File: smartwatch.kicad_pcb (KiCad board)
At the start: 2 copper layers, 40 x 40 mm, 42 parts, among them IC2 NORA-B120-00B, J1 Conn_01x01_Pin, J2 Conn_01x01_Pin, J3 5022441530, J5 Conn_01x06_Pin, Q1 2N7002-7-F, U1 MAX17048G+T10, U10 AP2127K-1.8, U2 AP2112K-3.3TRG1, U3 MAX30102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

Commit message: charging circuit complete
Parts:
- removed BT1: Battery_Cell, Capacitor_SMD:C_1812_4532Metric
- removed C10, C6: 100uF, Capacitor_SMD:C_0402_1005Metric
- removed C2: 1uF, Capacitor_SMD:C_0402_1005Metric
- removed D1: LED_GREEN, LED_SMD:LED_0402_1005Metric
- removed J5: Conn_01x06_Pin, Connector_PinHeader_2.54mm:PinHeader_1x06_P2.54mm_Vertical
- removed R1: 3.3k, Resistor_SMD:R_0402_1005Metric
- removed R12: 470, Resistor_SMD:R_0402_1005Metric
- removed R6: 5.1k, Resistor_SMD:R_0402_1005Metric
- removed U2: AP2112K-3.3TRG1, AP2112K-3-3TRG1:SOT_RG1_DIO
- removed U7: MCP73831-2-OT, Package_TO_SOT_SMD:SOT-23-5
- added BT3: Battery_Cell, Capacitor_SMD:C_1812_4532Metric, F.Cu at (149.9, 105.8)
- added C15: 100uF, Capacitor_SMD:C_0402_1005Metric, F.Cu at (158.3, 88.3)
- added C16: 4.7uF, Capacitor_Tantalum_SMD:CP_EIA-2012-12_Kemet-R, F.Cu at (159.9, 87.5)
- added C18: 0.1uF, Capacitor_SMD:C_0402_1005Metric, F.Cu at (171.3, 106.2)
- added C19: 4.7uF, Capacitor_SMD:C_0402_1005Metric, F.Cu at (146.9, 106.0)
- added D5: LBAT54XV2T1G, Diode_SMD:D_SOD-523, F.Cu at (160.1, 97.0)
- added D6: LED_GREEN, LED_SMD:LED_0402_1005Metric, F.Cu at (144.0, 99.6)
- added IC1: W25N01GVZEIG, W25N01GVZEIG_TR:SON127P800X600X80-9N-D, F.Cu at (167.1, 102.3)
- added J4: Conn_01x03_Pin, Connector_PinSocket_2.54mm:PinSocket_1x03_P2.54mm_Vertical, F.Cu at (168.4, 107.6)
- added J6: Conn_01x01_Pin, Connector_PinSocket_2.54mm:PinSocket_1x01_P2.54mm_Vertical, F.Cu at (159.7, 105.6)
- added Q2: NTR1P02T1G, Package_TO_SOT_SMD:SOT-23, F.Cu at (157.2, 97.3)
- added Q6: NTR1P02T1G, Package_TO_SOT_SMD:SOT-23, F.Cu at (157.2, 100.8)
- added R14: 3.3k, Resistor_SMD:R_0603_1608Metric, F.Cu at (171.0, 82.8)
- added R16: 5.1k, Resistor_SMD:R_0603_1608Metric, F.Cu at (160.5, 102.2)
- added R17: 5.1k, Resistor_SMD:R_0402_1005Metric, F.Cu at (148.0, 101.2)
- added R18: 470, Resistor_SMD:R_0402_1005Metric, F.Cu at (146.2, 99.6)
- added REF**: MountingHole_2.2mm_M2_Pad, MountingHole:MountingHole_2.2mm_M2_Pad, F.Cu at (159.1, 110.3)
- added REF**: MountingHole_2.2mm_M2_Pad, MountingHole:MountingHole_2.2mm_M2_Pad, F.Cu at (159.1, 74.9)
- added U11: MCP73831-2-OT, Package_TO_SOT_SMD:SOT-23-5, F.Cu at (145.1, 101.9)
- C1: value 4.7uF -> 1uF
- J1: value Conn_01x01_Pin -> Charging_Pad-
- J2: value Conn_01x01_Pin -> Charging_Pad+
- Q1: value 2N7002-7-F -> 2N7002
- R13: footprint Resistor_SMD:R_0402_1005Metric -> Resistor_SMD:R_0603_1608Metric
- U3: moved to B.Cu
- U8: value W25Q128JVS -> AP2112K-3.3TRG1; footprint Package_SO:SOIC-8_5.23x5.23mm_P1.27mm -> AP2112K-3-3TRG1:SOT_RG1_DIO
- moved C12 48.5 mm to (153.2, 109.2), turned to -90 degrees
- moved C7 47.6 mm to (155.5, 109.2), turned to -90 degrees
- moved C8 47.2 mm to (154.4, 109.2), turned to -90 degrees
- moved U10 43.1 mm to (154.2, 105.4)
- moved U3 35.7 mm to (159.1, 92.5), turned to 180 degrees
- moved U1 23.7 mm to (174.3, 101.2), turned to 90 degrees
- moved R5 23.2 mm to (153.5, 100.0), turned to -90 degrees
- moved R7 21.5 mm to (152.5, 100.0), turned to -90 degrees
- moved R8 18.3 mm to (149.9, 99.6), turned to 180 degrees
- moved R10 18.2 mm to (147.0, 85.6)
- moved U8 13.6 mm to (159.1, 92.5), turned to 90 degrees
- moved C1 11.8 mm to (153.6, 103.0)
- moved C4 6.72 mm to (178.5, 77.3)
- moved C5 6.72 mm to (178.5, 79.3)
- moved J3 4.00 mm to (159.0, 81.3), turned to 180 degrees
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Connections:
- C1 pad 1: Net-(BT1-+) -> VBUS
- IC2 pad D1: unconnected-(IC2-P0.15/IO2-PadD1) -> /FLASH_IO2
- IC2 pad D2: unconnected-(IC2-P0.13/IO0-PadD2) -> /FLASH_IO0
- IC2 pad E1: unconnected-(IC2-P0.18/CSN-PadE1) -> /FLASH_CS
- IC2 pad E2: unconnected-(IC2-P0.14/IO1-PadE2) -> /FLASH_IO1
- IC2 pad E8: unconnected-(IC2-P0.05/AIN1_-PadE8) -> /BACKLIGHT_EN
- IC2 pad F1: unconnected-(IC2-P0.17/SCK-PadF1) -> /FLASH_CLK
- IC2 pad F2: unconnected-(IC2-P0.16/IO3-PadF2) -> /FLASH_IO3
- IC2 pad G9: unconnected-(IC2-P1.13-PadG9) -> /SCL
- IC2 pad H9: unconnected-(IC2-P1.11_-PadH9) -> /SDA
- J2 pad 1: Net-(D2-A) -> VBUS
- R13 pad 1: /AC_SCL -> /SDA
- R13 pad 2: +3.3V -> VSYS
- U1 pad 1: Net-(BT1-+) -> GND
- U1 pad 2: Net-(BT1-+) -> /BAT+
- U1 pad 3: GND -> /BAT+
- U1 pad 7: /GAUGE_SCL -> /SCL
- U1 pad 8: /GAUGE_SDA -> /SDA
- U10 pad 1: VSYS -> /BAT+
- U3 pad 2: /AC_SCL -> /SCL
- U3 pad 3: /AC_SDA -> /SDA
- U8 pad 1: /FLASH_CS -> Net-(D5-K)
- U8 pad 2: /SD_DO -> GND
- U8 pad 3: /SD_WP -> Net-(D5-K)
- U8 pad 4: GND -> unconnected-(U8-NC-Pad4)
- U8 pad 5: /SD_DI -> VSYS
- U9 pad 1: /AC_SCL -> /SCL
- U9 pad 4: /AC_SDA -> /SDA
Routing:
- net /BAT+: track 0.00 -> 42.3 mm, vias 0 -> 2
- net VBUS: track 0.00 -> 36.3 mm, vias 0 -> 4
- net VSYS: track 8.00 -> 19.1 mm
- net Net-(U10-VOUT): track 0.00 -> 8.22 mm
- net Net-(D5-K): track 0.00 -> 6.96 mm
- net Net-(D2-K): track 6.09 -> 0.00 mm
- net Net-(R8-Pad1): track 0.00 -> 2.70 mm
- net Net-(R7-Pad1): track 0.00 -> 2.65 mm
- net Net-(R5-Pad1): track 0.00 -> 2.64 mm
- net Net-(Q2-D): track 0.00 -> 2.59 mm
- net Net-(U11-PROG): track 0.00 -> 2.04 mm
- net Net-(D6-K): track 0.00 -> 1.58 mm
- net Net-(U5-Pad16): track 0.00 -> 1.00 mm

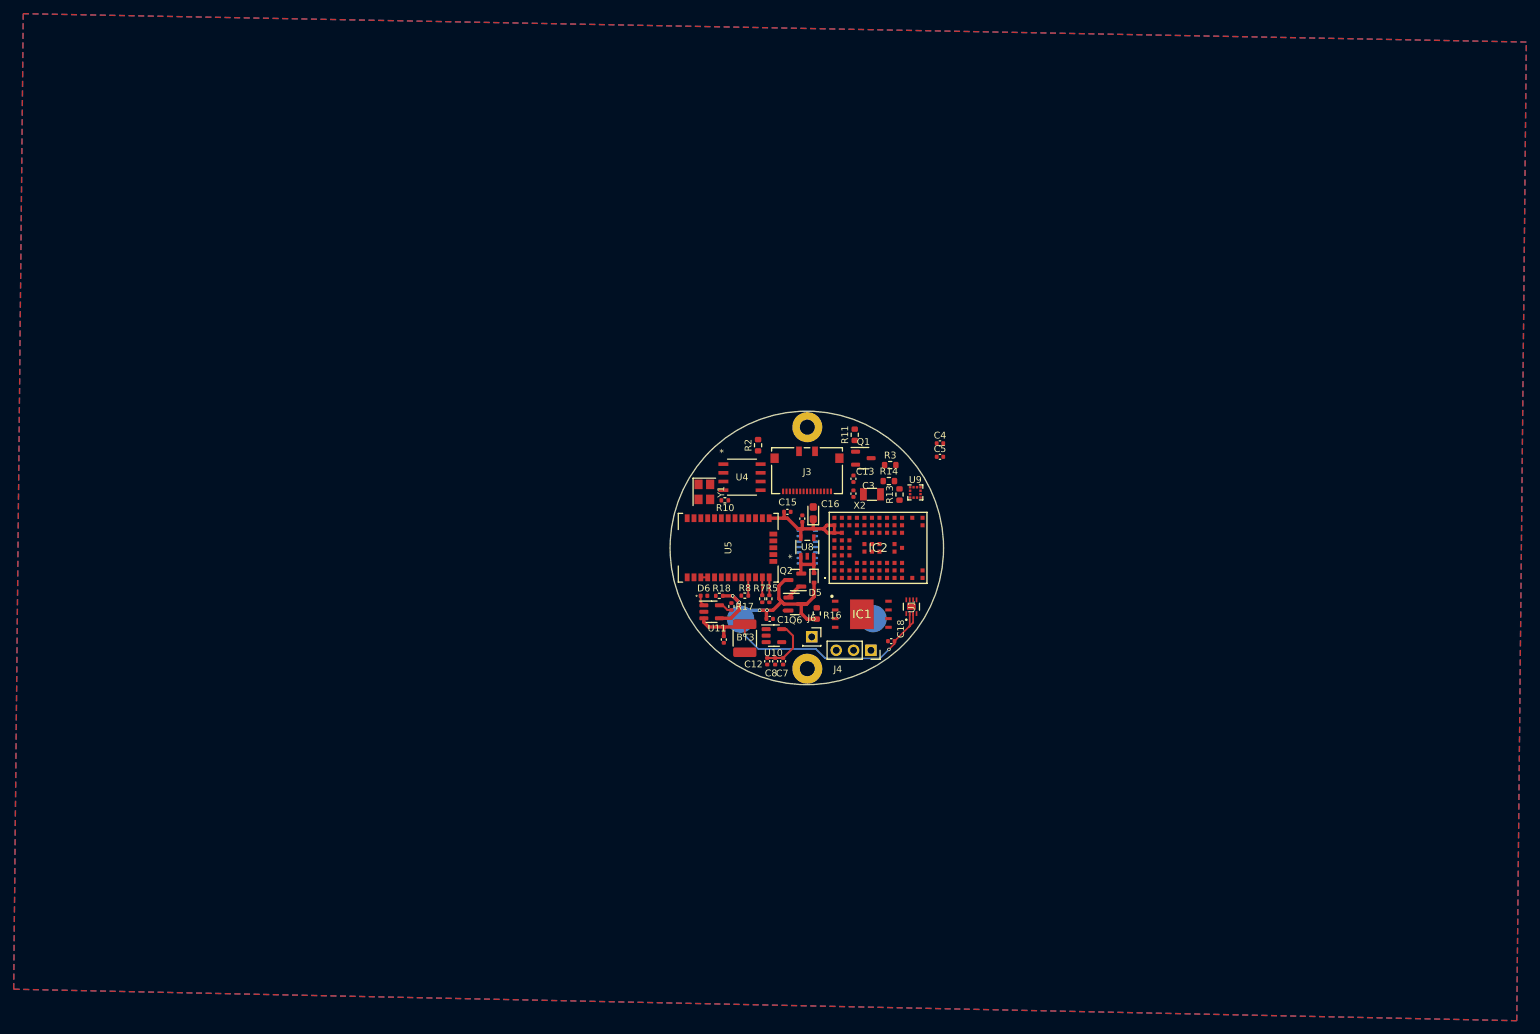
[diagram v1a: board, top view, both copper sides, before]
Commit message: switched to 4 layers
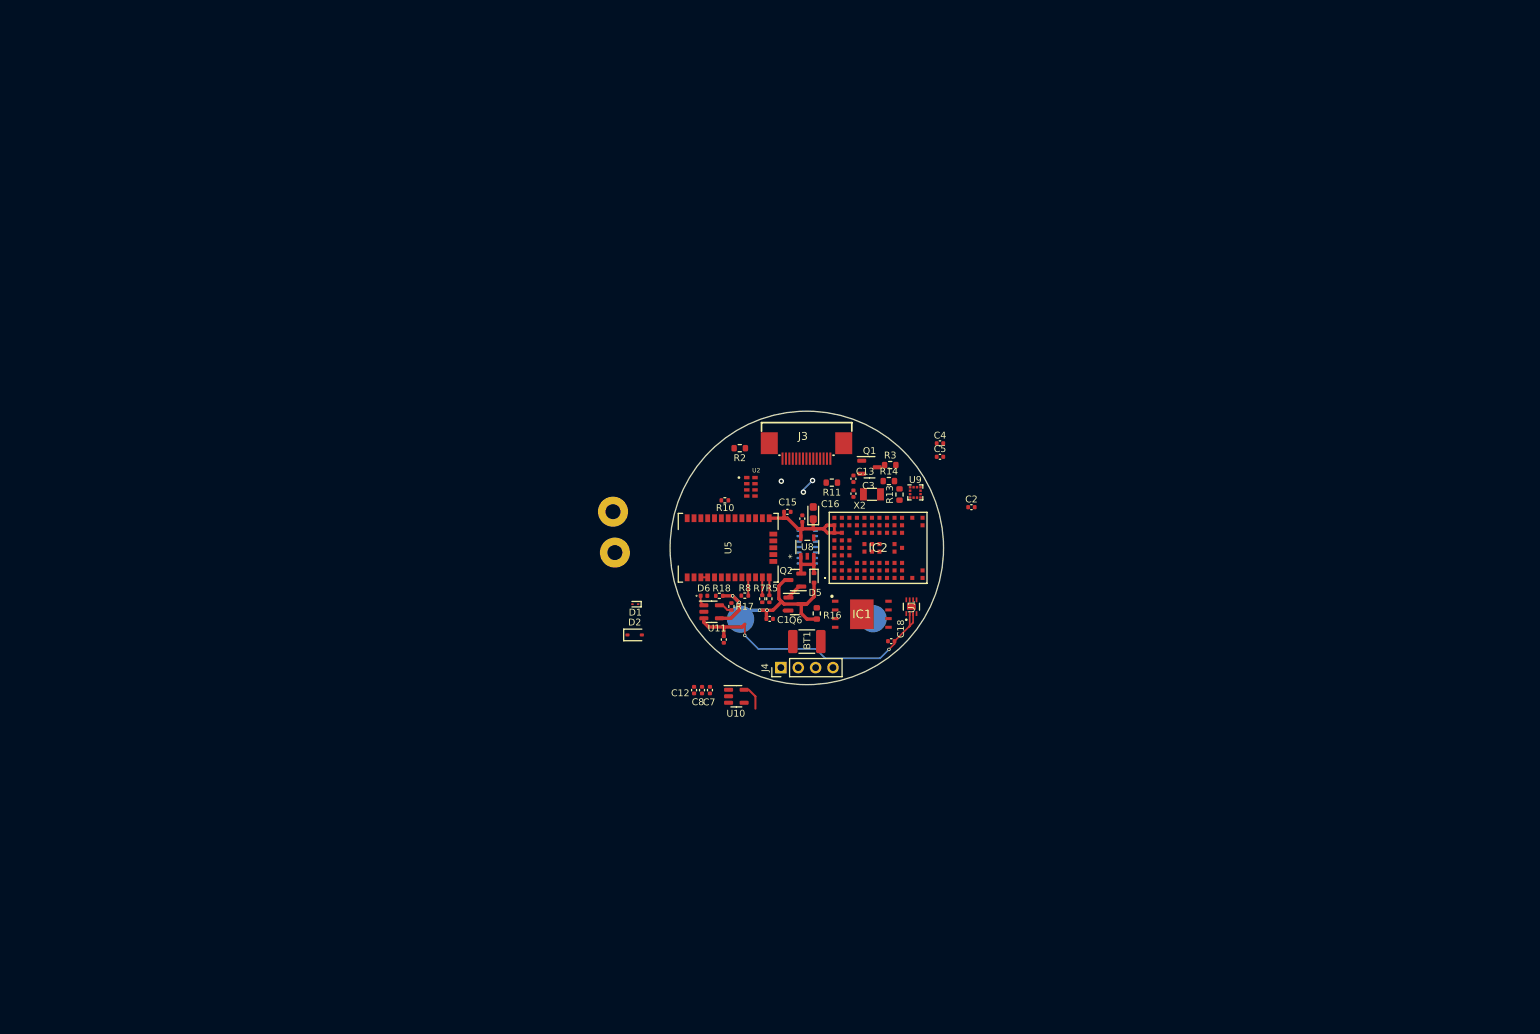
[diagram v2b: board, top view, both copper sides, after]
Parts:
- removed BT3: Battery_Cell, Capacitor_SMD:C_1812_4532Metric
- removed J6: Conn_01x01_Pin, Connector_PinSocket_2.54mm:PinSocket_1x01_P2.54mm_Vertical
- removed U4: DS1302Z+T&R, DS1302Z+T&R:21-0041B_8_MXM
- removed Y1: 32.768kHz, Crystal:Crystal_SMD_TXC_7M-4Pin_3.2x2.5mm
- added BT1: Battery_Cell, Capacitor_SMD:C_1812_4532Metric, F.Cu at (159.0, 106.3)
- added C2: 100uF, Capacitor_SMD:C_0402_1005Metric, F.Cu at (183.1, 86.6)
- added D1: CDBQC0130L-HF, Diode_SMD:D_SOD-923, F.Cu at (133.9, 100.8)
- added D2: CUS08F30,H3F, Diode_SMD:D_SOD-323, F.Cu at (133.8, 105.3)
- added U2: RV-3028-C7_32.768KHZ_1PPM-TA-QC, RV_3028_C7_32_768KHZ_1PPM_TA_QC:IC_RV-3028-C7_32.768KHZ_1PPM-TA-QC, F.Cu at (150.8, 83.7)
- J3: value 5022441530 -> DS1020-09-15VBT1A; footprint MOLEX_5022441530:CONN_502244-1530_MOL -> DISPLAY_CONNECTOR:FPC-SMD_P0.50-15P_LSXJ-H2.0-15P
- J4: value Conn_01x03_Pin -> Conn_01x04_Pin; footprint Connector_PinSocket_2.54mm:PinSocket_1x03_P2.54mm_Vertical -> Connector_PinHeader_2.54mm:PinHeader_1x04_P2.54mm_Vertical
- R11: value 10k -> 1M
- moved REF** 32.9 mm to (130.9, 93.3)
- moved REF** 31.0 mm to (130.7, 87.3)
- moved J4 13.4 mm to (155.2, 110.1), turned to 90 degrees
- moved C12 11.5 mm to (142.5, 113.4)
- moved C8 11.5 mm to (143.7, 113.4)
- moved C7 11.5 mm to (144.8, 113.4)
- moved U10 10.4 mm to (148.7, 114.3)
- moved R11 7.76 mm to (162.7, 83.0), turned to 180 degrees
- moved J3 2.89 mm to (159.0, 78.4), turned to 0 degrees
- moved R2 2.71 mm to (149.2, 78.0), turned to 180 degrees
- moved Q1 1.61 mm to (168.2, 80.8)
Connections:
- net Net-(IC2-P0.00/XL1) renamed /XL1
- net Net-(IC2-P0.01/XL2) renamed /XL2
- IC2 pad A1: unconnected-(IC2-VSS_1-PadA1) -> GND
- IC2 pad A9: unconnected-(IC2-VSS_2-PadA9) -> GND
- IC2 pad B2: unconnected-(IC2-VSS_3-PadB2) -> GND
- IC2 pad B8: unconnected-(IC2-VSS_4-PadB8) -> GND
- IC2 pad C8: unconnected-(IC2-P0.22-PadC8) -> /RTC_CLK
- IC2 pad D7: unconnected-(IC2-P0.23-PadD7) -> /RTC_EVI
- IC2 pad E4: unconnected-(IC2-VSS_5-PadE4) -> GND
- IC2 pad E5: unconnected-(IC2-VSS_6-PadE5) -> GND
- IC2 pad F7: unconnected-(IC2-P1.07-PadF7) -> /RTC_INT
- IC2 pad K2: unconnected-(IC2-VSS_9-PadK2) -> GND
- IC2 pad K3: unconnected-(IC2-VSS_10-PadK3) -> GND
- IC2 pad K5: unconnected-(IC2-VSS_11-PadK5) -> GND
- IC2 pad K7: unconnected-(IC2-VSS_12-PadK7) -> GND
- IC2 pad K8: unconnected-(IC2-VSS_13-PadK8) -> GND
- IC2 pad L1: unconnected-(IC2-VSS_14-PadL1) -> GND
- IC2 pad L9: unconnected-(IC2-VSS_15-PadL9) -> GND
- IC2 pad M1: unconnected-(IC2-VSS_16-PadM1) -> GND
- IC2 pad M2: unconnected-(IC2-VSS_17-PadM2) -> GND
- IC2 pad M8: unconnected-(IC2-VSS_18-PadM8) -> GND
- IC2 pad M9: unconnected-(IC2-VSS_19-PadM9) -> GND
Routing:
- net GND: track 0.00 -> 10.6 mm, vias 0 -> 3
- net Net-(U10-VOUT): track 8.22 -> 3.17 mm
- added copper zone on In1.Cu, net GND
- added copper zone on In2.Cu, net GND
- removed copper zone on B.Cu, net GND
- removed copper zone on F.Cu, net GND
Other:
- copper layers 2 -> 4

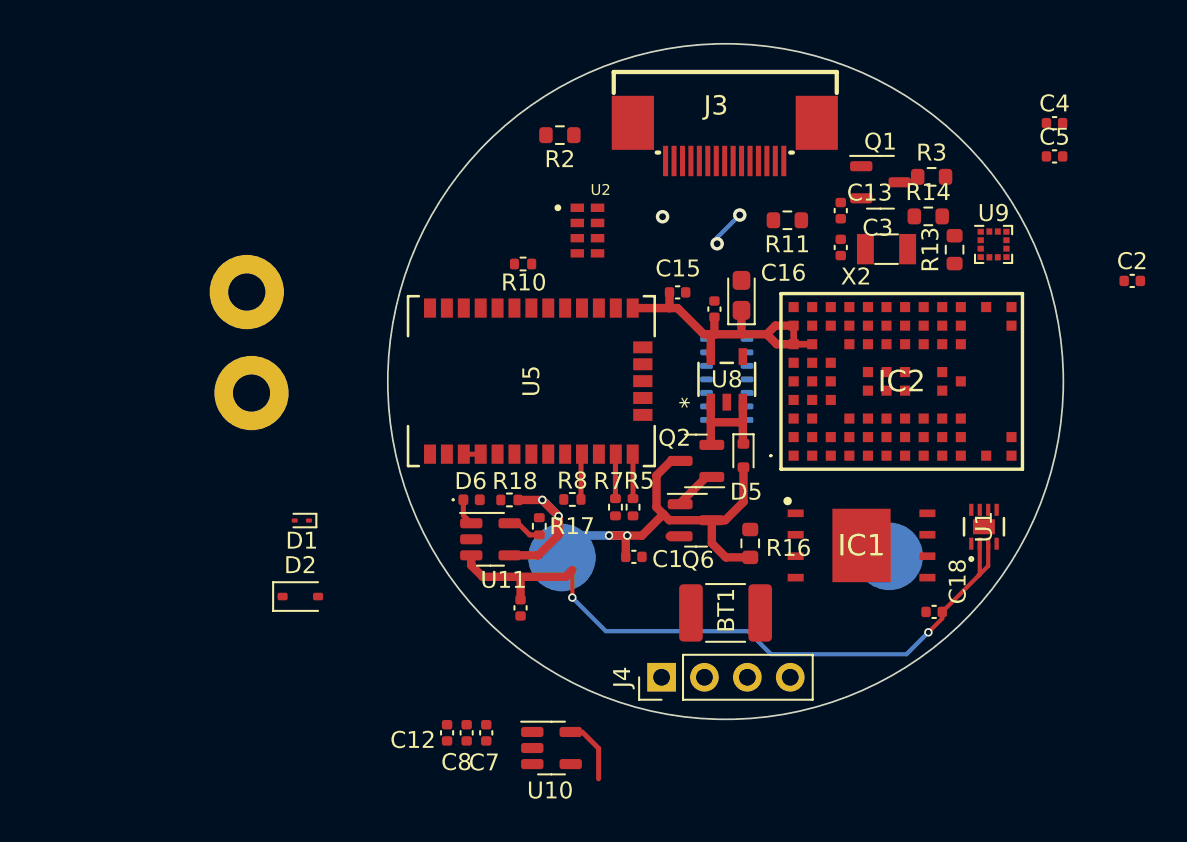
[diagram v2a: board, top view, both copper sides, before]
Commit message: worked on power traces & added mounting holes
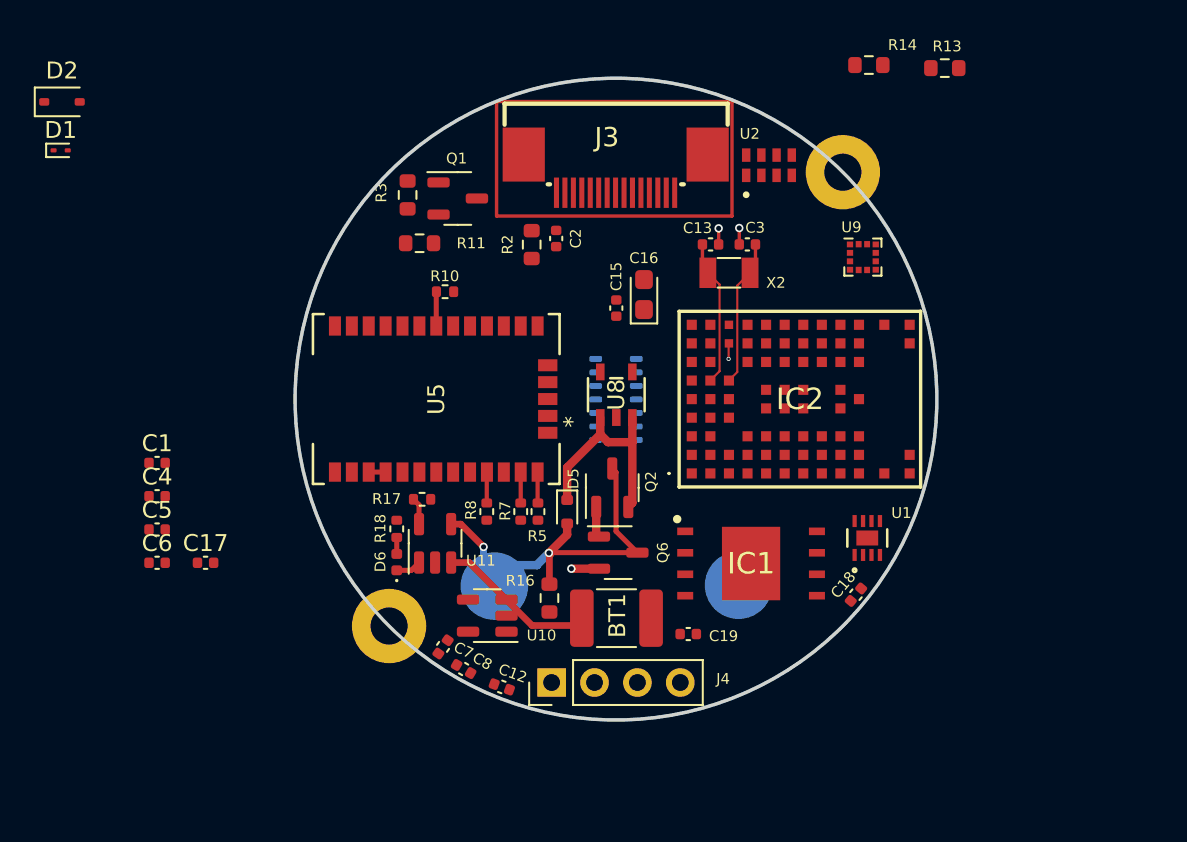
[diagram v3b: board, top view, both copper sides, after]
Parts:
- removed REF** (x2): MountingHole_2.2mm_M2_Pad, MountingHole:MountingHole_2.2mm_M2_Pad
- added ?: , , F.Cu at (165.9, 80.2)
- added ?: , , F.Cu at (139.1, 107.1)
- added C6: 1uF, Capacitor_SMD:C_0402_1005Metric, F.Cu at (125.3, 103.3)
- Q2, Q6: value NTR1P02T1G -> AO3401; footprint Package_TO_SOT_SMD:SOT-23 -> Package_TO_SOT_SMD:SOT-23-3
- R13, R14: value 3.3k -> 4.7k
- R2: value 22 -> 100
- moved C4 57.5 mm to (125.3, 99.4)
- moved C5 57.5 mm to (125.3, 101.4)
- moved C2 34.2 mm to (149.0, 84.1), turned to -90 degrees
- moved D2 32.5 mm to (119.7, 76.0)
- moved C17 32.2 mm to (128.2, 103.3)
- moved R3 31.0 mm to (140.2, 81.5), turned to 90 degrees
- moved C1 28.8 mm to (125.3, 97.4)
- moved D1 26.2 mm to (119.6, 78.9), turned to 0 degrees
- moved Q1 25.0 mm to (143.1, 81.8)
- moved R11 21.8 mm to (140.9, 84.4)
- moved R16 12.3 mm to (148.6, 105.4), turned to -90 degrees
- moved U2 11.4 mm to (161.6, 79.8), turned to 90 degrees
- moved D5 11.0 mm to (149.6, 100.3)
- moved R13 10.8 mm to (172.0, 74.0), turned to 180 degrees
- moved C19 10.1 mm to (156.8, 107.5), turned to 0 degrees
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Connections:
- U10 pad 3: unconnected-(U10-EN-Pad3) -> /BAT+
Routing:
- net /BAT+: track 42.3 -> 11.6 mm, vias 2 -> 1
- net VSYS: track 19.1 -> 0.00 mm
- net VBUS: track 36.3 -> 24.1 mm, vias 4 -> 2
- net /XL1: track 0.00 -> 8.73 mm
- net /XL2: track 0.00 -> 8.72 mm
- net Net-(D5-K): track 6.96 -> 13.2 mm
- net Net-(U10-VOUT): track 3.17 -> 0.00 mm
- net Net-(R10-Pad2): track 0.00 -> 2.03 mm
- net Net-(D6-A): track 0.00 -> 0.98 mm
- net /RTC_CLK: track 0.00 -> 0.91 mm, vias 0 -> 1
- net Net-(R8-Pad1): track 2.70 -> 1.83 mm
- net Net-(R7-Pad1): track 2.65 -> 1.83 mm
- net Net-(R5-Pad1): track 2.64 -> 1.84 mm
- net Net-(Q2-D): track 2.59 -> 1.82 mm
- net GND: track 10.6 -> 10.3 mm, vias 3 -> 2
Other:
- board size 40 x 40 mm -> 38 x 38 mm
